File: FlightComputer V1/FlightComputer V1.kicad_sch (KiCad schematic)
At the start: 4 parts, among them U1 BMP280, U2 MPU-6050, U3 W25Q64

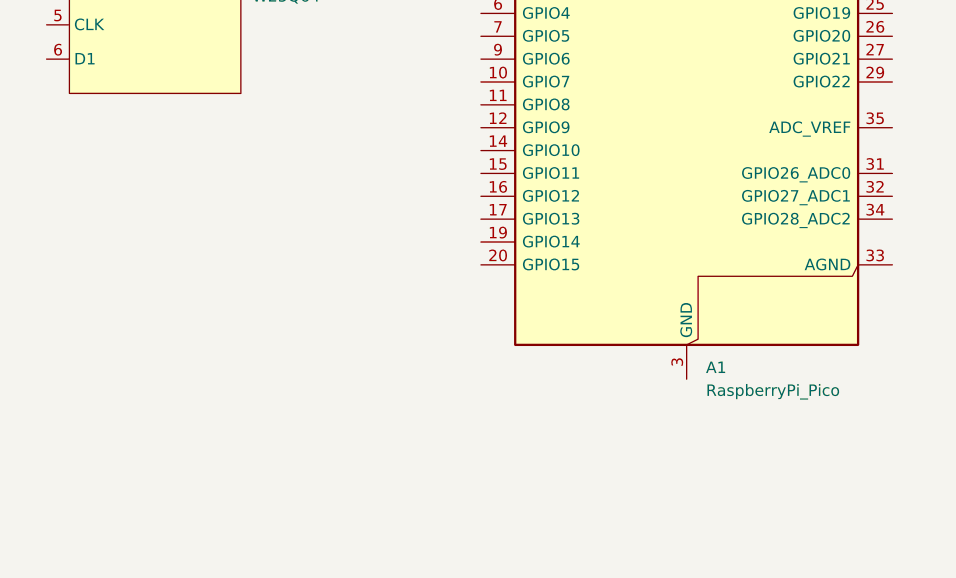
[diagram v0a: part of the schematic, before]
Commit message: All breakout boards
All breakout boards added + mosfets, have also changed pins to through holes 1.9mm dia and 1mm hole dia
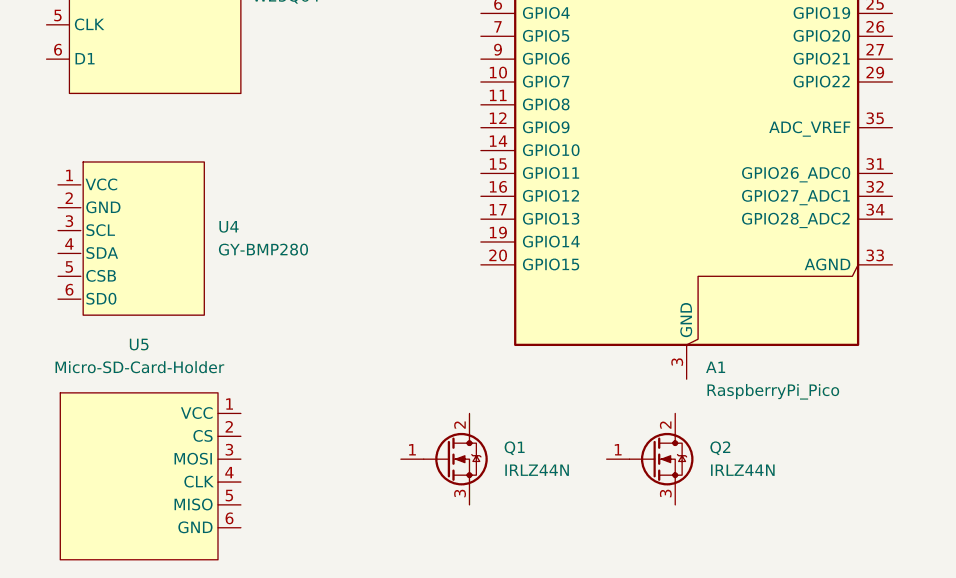
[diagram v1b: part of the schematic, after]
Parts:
- added Q1, Q2: IRLZ44N, Package_TO_SOT_THT:TO-220-3_Vertical, symbol Transistor_FET:IRLZ44N
- added U4: GY-BMP280, symbol FlightComputerV1Parts:GY-BMP280
- added U5: Micro-SD-Card-Holder, symbol FlightComputerV1Parts:Micro-SD-card-holder_

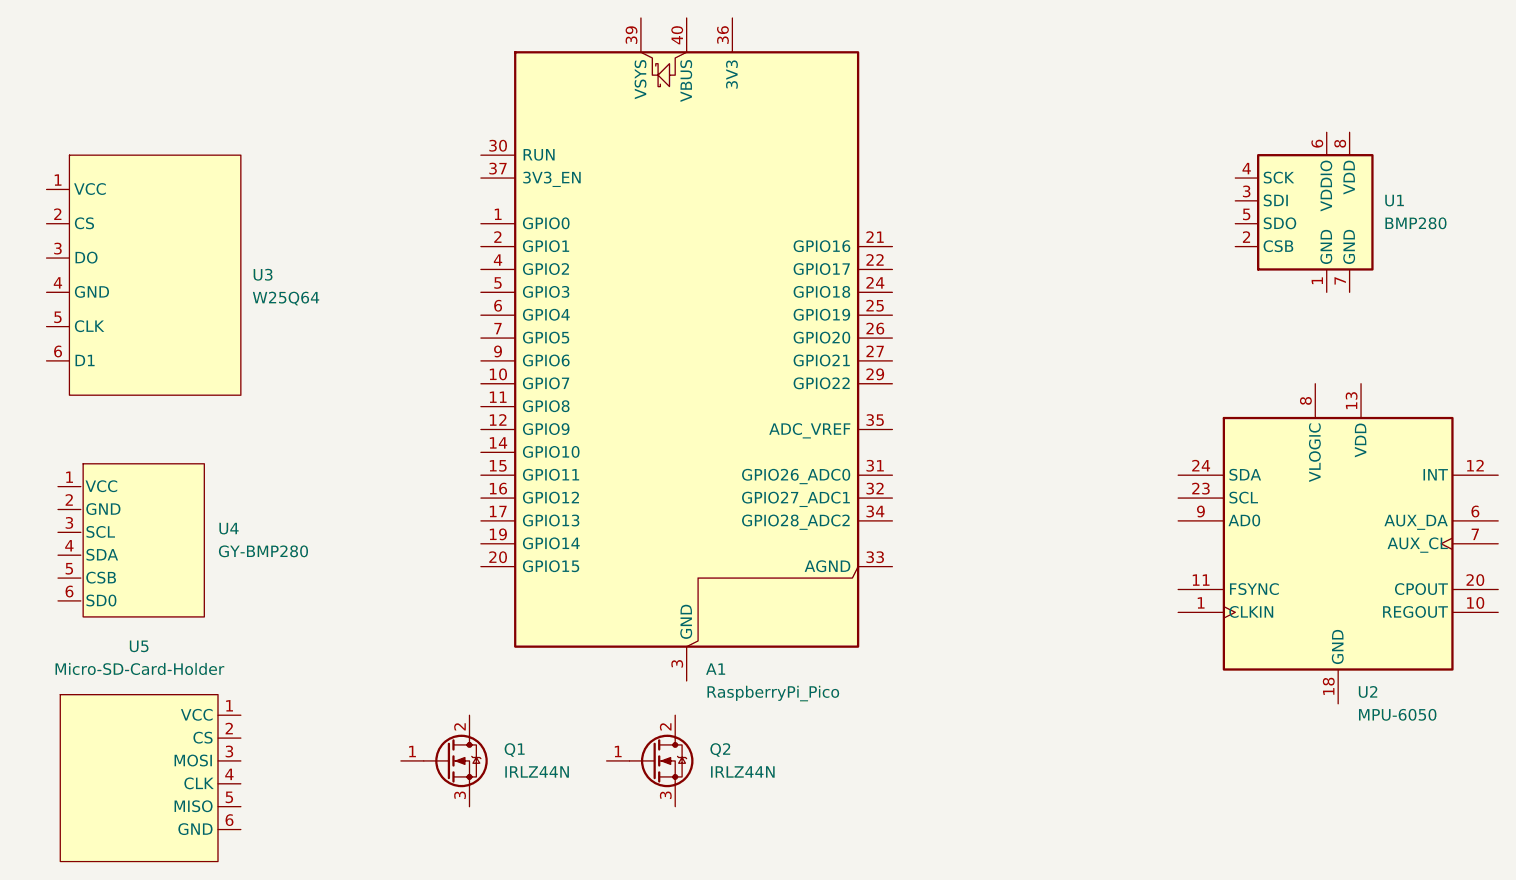
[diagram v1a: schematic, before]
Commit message: Split into sheets
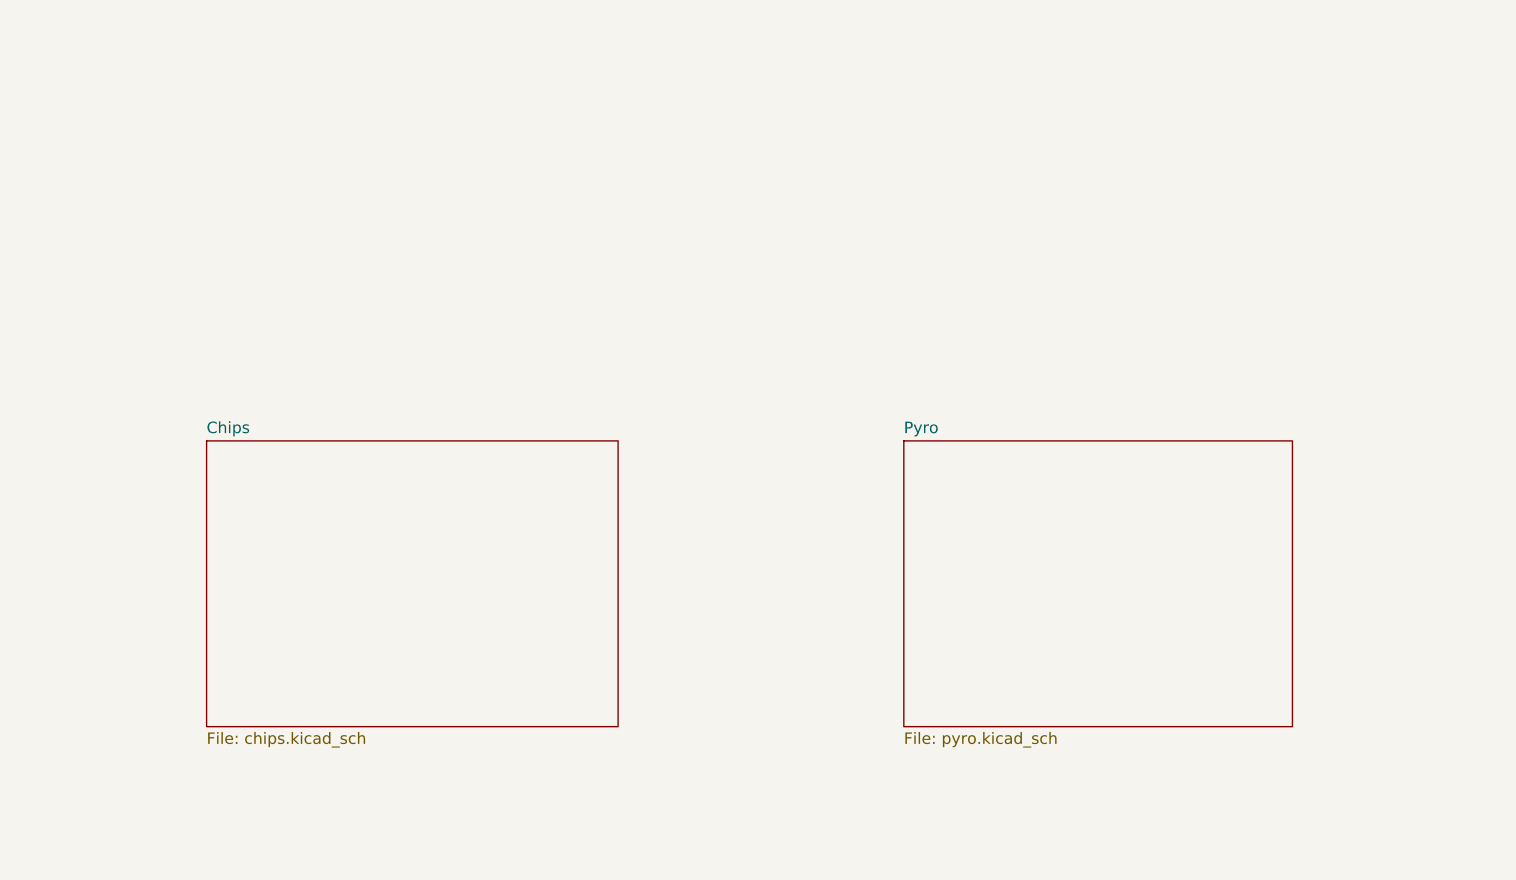
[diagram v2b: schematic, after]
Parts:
- removed A1: RaspberryPi_Pico, Module:RaspberryPi_Pico_Common_Unspecified, symbol MCU_Module:RaspberryPi_Pico
- removed Q1, Q2: IRLZ44N, Package_TO_SOT_THT:TO-220-3_Vertical, symbol Transistor_FET:IRLZ44N
- removed U1: BMP280, Package_LGA:Bosch_LGA-8_2x2.5mm_P0.65mm_ClockwisePinNumbering, symbol Sensor_Pressure:BMP280
- removed U2: MPU-6050, Sensor_Motion:InvenSense_QFN-24_4x4mm_P0.5mm, symbol Sensor_Motion:MPU-6050
- removed U3: W25Q64, FlightComputerV1_footprints:W25Q64, symbol FlightComputerV1Parts:DollaTek W25Q64
- removed U4: GY-BMP280, symbol FlightComputerV1Parts:GY-BMP280
- removed U5: Micro-SD-Card-Holder, symbol FlightComputerV1Parts:Micro-SD-card-holder_
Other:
- added sheet Chips (chips.kicad_sch)
- added sheet Pyro (pyro.kicad_sch)

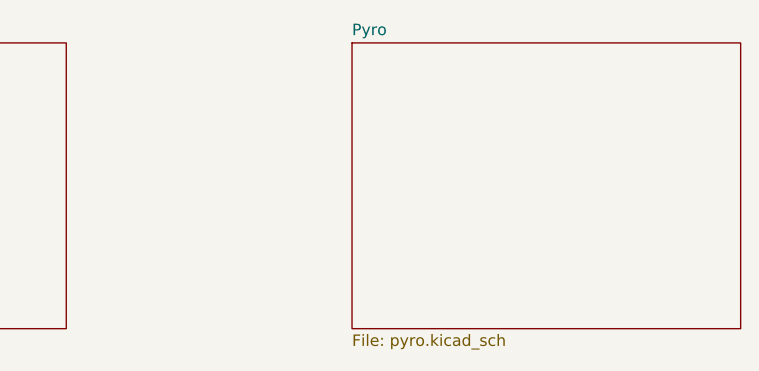
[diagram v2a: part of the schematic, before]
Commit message: add pyro
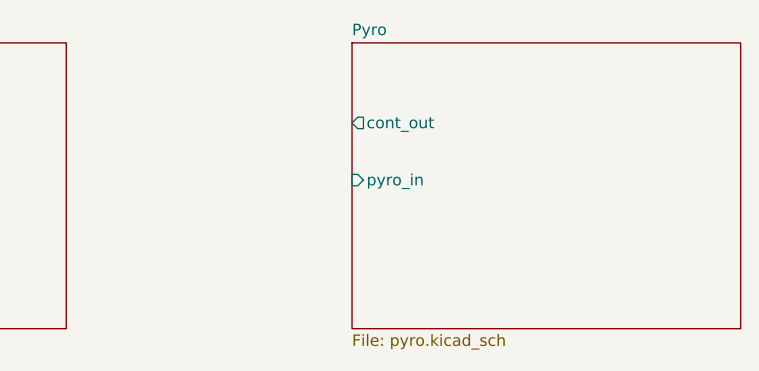
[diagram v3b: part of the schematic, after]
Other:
- sheet Pyro ports: added cont_out, pyro_in; removed none
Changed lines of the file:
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@@
+			)
+		)
+		(pin "cont_out" output
+			(at 165.1 78.74 180)
+			(effects
+				(font
+					(size 1.27 1.27)
+				)
+				(justify left)
+			)
+		)
+		(pin "pyro_in" input
+			(at 165.1 85.09 180)
+			(effects
+				(font
+					(size 1.27 1.27)
+				)
+				(justify left)
 			)
 		)
